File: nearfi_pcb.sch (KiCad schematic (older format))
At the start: 24 parts, among them J1 PWR_CONN, J2 CONN_PROG, Q1 MMBT3904, SW1 RESET, SW2 BOOT, U1 ESP32-S2-WROVER, U2 TLV1117-33

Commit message: Changed components and corrected errors
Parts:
- removed D1: NeoPixel_THT, LED_THT:LED_D5.0mm-4_RGB, symbol LED:NeoPixel_THT
- removed J2: CONN_PROG, Connector_PinHeader_2.54mm:PinHeader_1x04_P2.54mm_Vertical, symbol Connector_Generic:Conn_01x04
- removed SW1: RESET, Button_Switch_SMD:SW_SPST_TL3342, symbol Switch:SW_Push
- added D1: WS2812B, LED_SMD:LED_WS2812B_PLCC4_5.0x5.0mm_P3.2mm, symbol LED:WS2812B
- added J3: CONN_PROG, Connector_PinHeader_2.54mm:PinHeader_2x03_P2.54mm_Vertical, symbol Connector_Generic:Conn_02x03_Odd_Even
- BZ1: footprint Buzzer_Beeper:Buzzer_Murata_PKMCS0909E4000-R1 -> Buzzer_Beeper:Buzzer_12x9.5RM7.6
- SW1: renamed from SW2; value BOOT -> FUNCTION; footprint Button_Switch_SMD:SW_SPST_TL3342 -> Button_Switch_THT:SW_Tactile_SPST_Angled_PTS645Vx31-2LFS
- renumbered C5 to C2, C6 to C3, C7 to C5, C10 to C6, R2 to R1, R4 to R2, R1 to R4
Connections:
- net +3V3: now also D1.1 (VDD), J3.1 (Pin_1)
- net BUZZER: now also U1.7 (IO04); no longer U1.11 (IO08)
- net GND: now also D1.3 (VSS), J3.6 (Pin_6)
- net RGB: now also U1.32 (IO38), D1.4 (DIN); no longer U1.39 (IO45)
- net RXD: now also J3.3 (Pin_3)
- net TXD: now also J3.5 (Pin_5)
- net FUNC: now reaches U1.27 (IO33)
- net FUNC: now also SW1.2
- net BOOT: now reaches U1.3 (IO00)
- net BOOT: now also J3.4 (Pin_4); no longer SW1.2
- net RESET: now reaches C4.2, R2.1, U1.41 (EN)
- net RESET: now also J3.2 (Pin_2)
- no-connect marks 36 -> 35
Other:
- note added: "Connectors and switches"
- note added: "Decoupling capacitors"
- note added: "Note: \n- C5 and C6 should be tantalum capacitors"
- note removed: "Connectors"
- note removed: "Note: \n- C7 and C10 should be tantalum capacitors"
- moved on the sheet: C2, C3, C4, J1, R2, R3, SW1

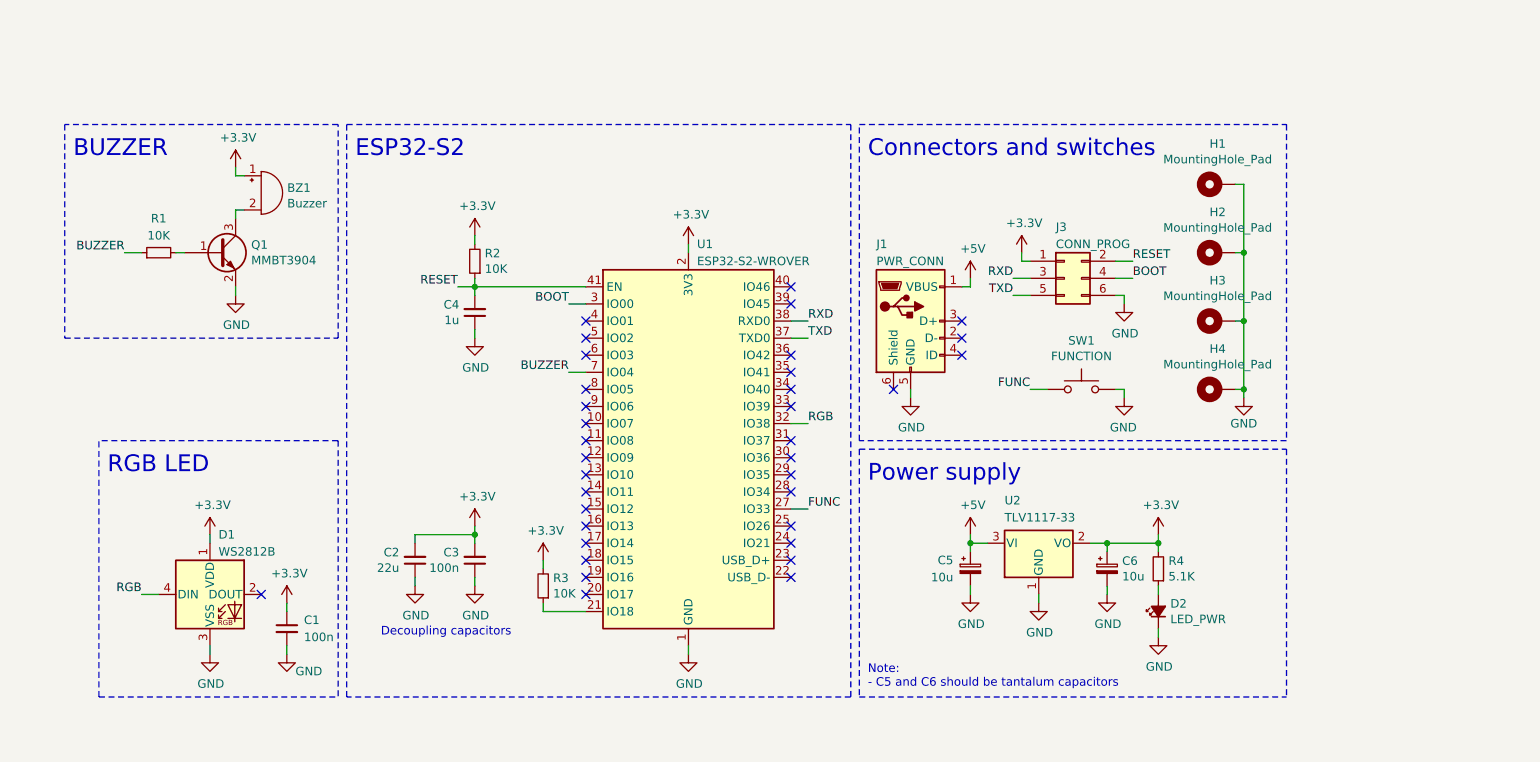
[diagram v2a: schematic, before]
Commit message: Added LCSC parts number and new ESP32-S2-WROOM symbol
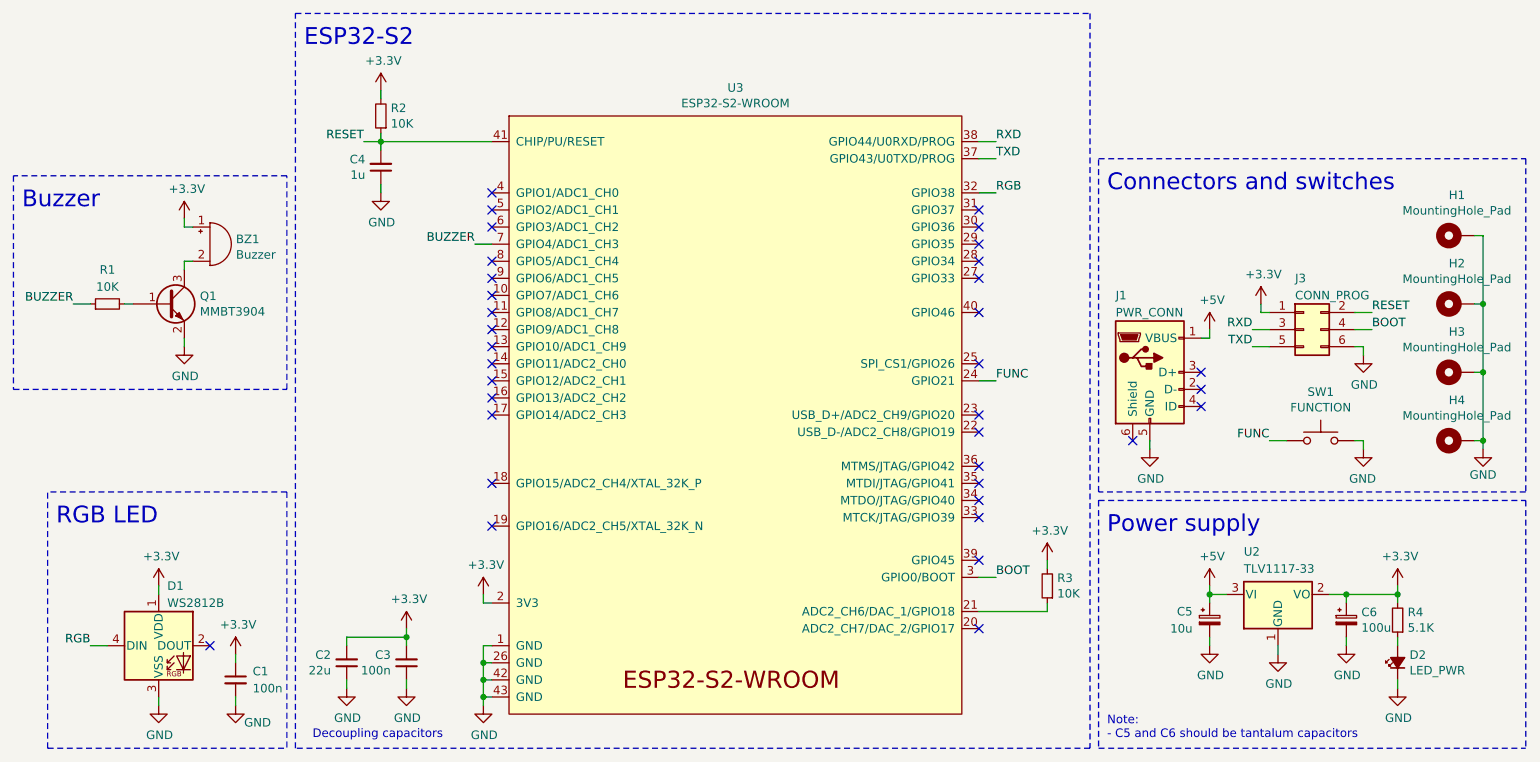
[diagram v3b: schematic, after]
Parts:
- removed U1: ESP32-S2-WROVER, RF_Module:ESP32-S2-WROVER, symbol RF_Module:ESP32-S2-WROVER
- added U3: ESP32-S2-WROOM, Espressif:ESP32-S2-WROOM, symbol Espressif:ESP32-S2-WROOM
- C1, C3: LCSC (none) -> C49678
- C2: LCSC (none) -> C45783
- C4: LCSC (none) -> C28323
- C5: footprint Capacitor_Tantalum_SMD:CP_EIA-2012-15_AVX-P_Pad1.30x1.05mm_HandSolder -> Capacitor_Tantalum_SMD:CP_EIA-3216-18_Kemet-A_Pad1.58x1.35mm_HandSolder; LCSC (none) -> C7171
- C6: value 10u -> 100u; footprint Capacitor_Tantalum_SMD:CP_EIA-2012-15_AVX-P_Pad1.30x1.05mm_HandSolder -> Capacitor_Tantalum_SMD:CP_EIA-3528-21_Kemet-B_Pad1.50x2.35mm_HandSolder; LCSC (none) -> C16133
- D1: LCSC (none) -> C2761795
- D2: LCSC (none) -> C84256
- J1: LCSC (none) -> C132560
- Q1: LCSC (none) -> C20526
- R1, R2, R3: LCSC (none) -> C17414
- R4: LCSC (none) -> C27834
- U2: LCSC (none) -> C37359
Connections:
- net +3V3: now also U3.2 (3V3)
- net BOOT: now also U3.3 (GPIO0/BOOT)
- net BUZZER: now also U3.7 (GPIO4/ADC1_CH3)
- net FUNC: now also U3.24 (GPIO21)
- net GND: now also U3.1 (GND), U3.26 (GND), U3.42 (GND), U3.43 (GND)
- net RESET: now also U3.41 (CHIP/PU/RESET)
- net RGB: now also U3.32 (GPIO38)
- net RXD: now also U3.38 (GPIO44/U0RXD/PROG)
- net TXD: now also U3.37 (GPIO43/U0TXD/PROG)
- net at R3.1: now also U3.21 (ADC2_CH6/DAC_1/GPIO18)
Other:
- note added: "Buzzer\n"
- note removed: "BUZZER"
- moved on the sheet: BZ1, C1, C2, C3, C4, C5, C6, D1, D2, H1, H2, H3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
